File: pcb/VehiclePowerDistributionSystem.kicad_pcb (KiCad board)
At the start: 4 copper layers, 70 x 70 mm, 84 parts, among them J1 B4B-XH-A, J2 B4B-XH-A, J3 B4B-XH-A, J4 B8B-XH-A, J5 B2B-XH-A, J6 FFC2B28-24-G, J7 B2B-XH-A, J8 B2B-XH-A, U1 TMC2209-LA-T, U2 TMC2209-LA-T, U3 TMC2209-LA-T, U4 D24V7F5, U5 D24V7F3, U6 TPS22810DRV, U7 TPS22810DRV

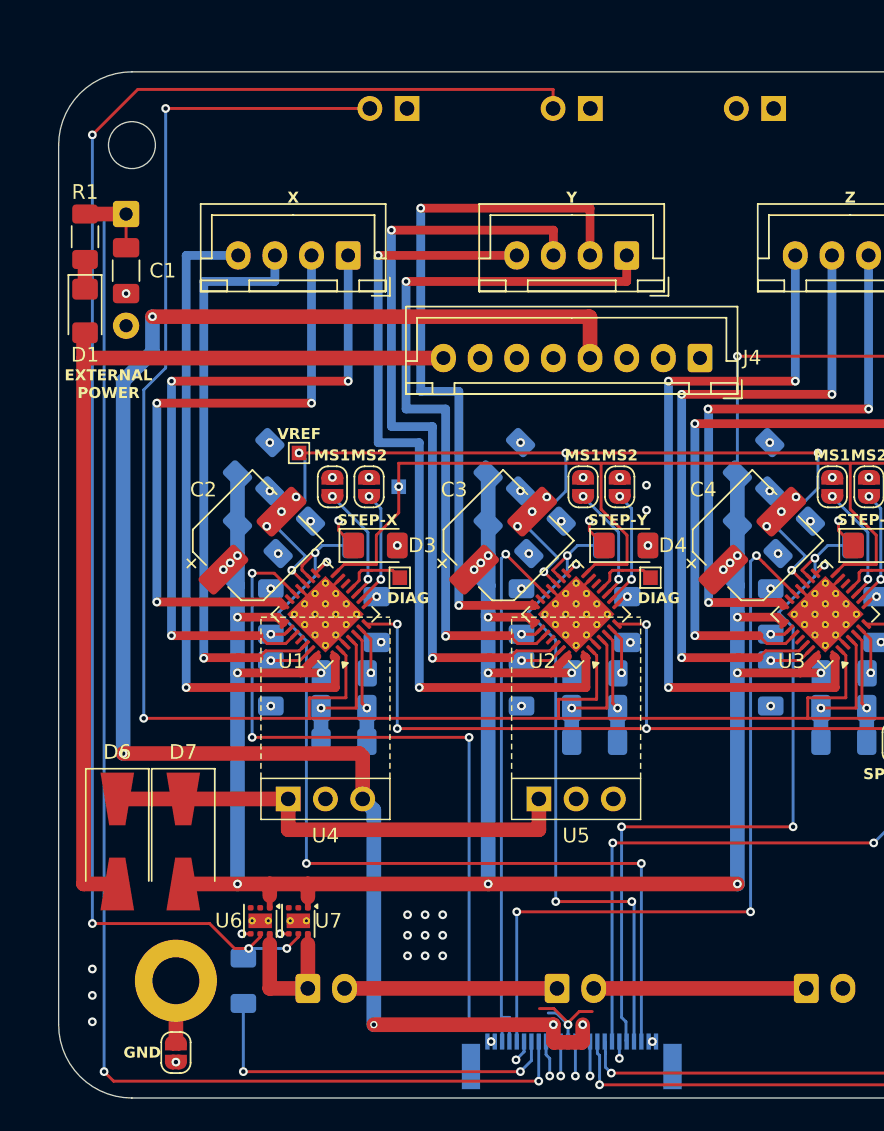
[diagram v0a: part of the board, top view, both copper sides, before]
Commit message: Moved D24V7Fx regulators on `VehiclePowerDistributionSystem` to account for heat-sinks of TMC2209s.
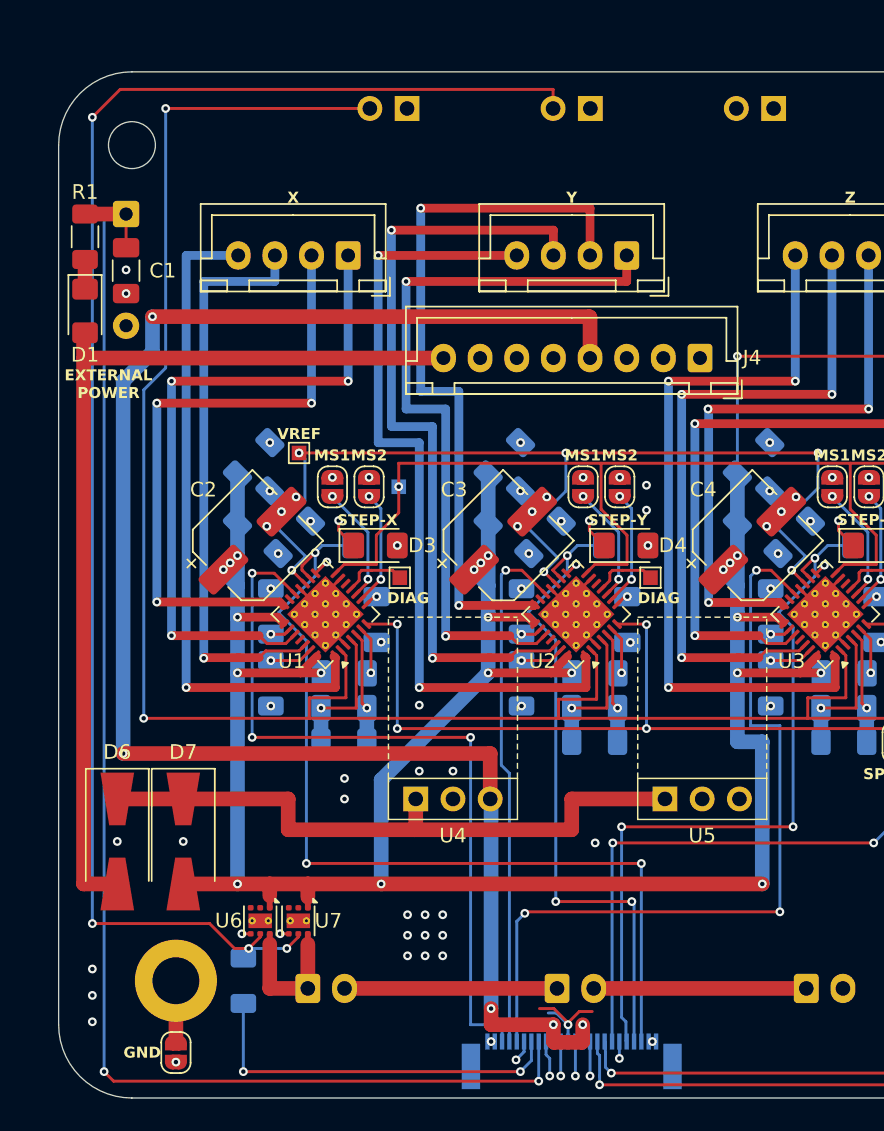
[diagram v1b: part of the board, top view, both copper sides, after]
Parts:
- moved U4 8.70 mm to (141.9, 114.6)
- moved U5 8.60 mm to (158.9, 114.6)
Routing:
- net Net-(D6-K): track 33.0 -> 43.7 mm
- net +MOTOR: track 191.0 -> 197.4 mm
- net motor_direction_z: track 53.0 -> 55.2 mm
- net motor_direction_y: track 37.8 -> 35.9 mm
- net Net-(JP10-B): track 104.4 -> 105.1 mm
- net +5V: track 117.2 -> 117.7 mm
- net +3.3V: vias 30 -> 39

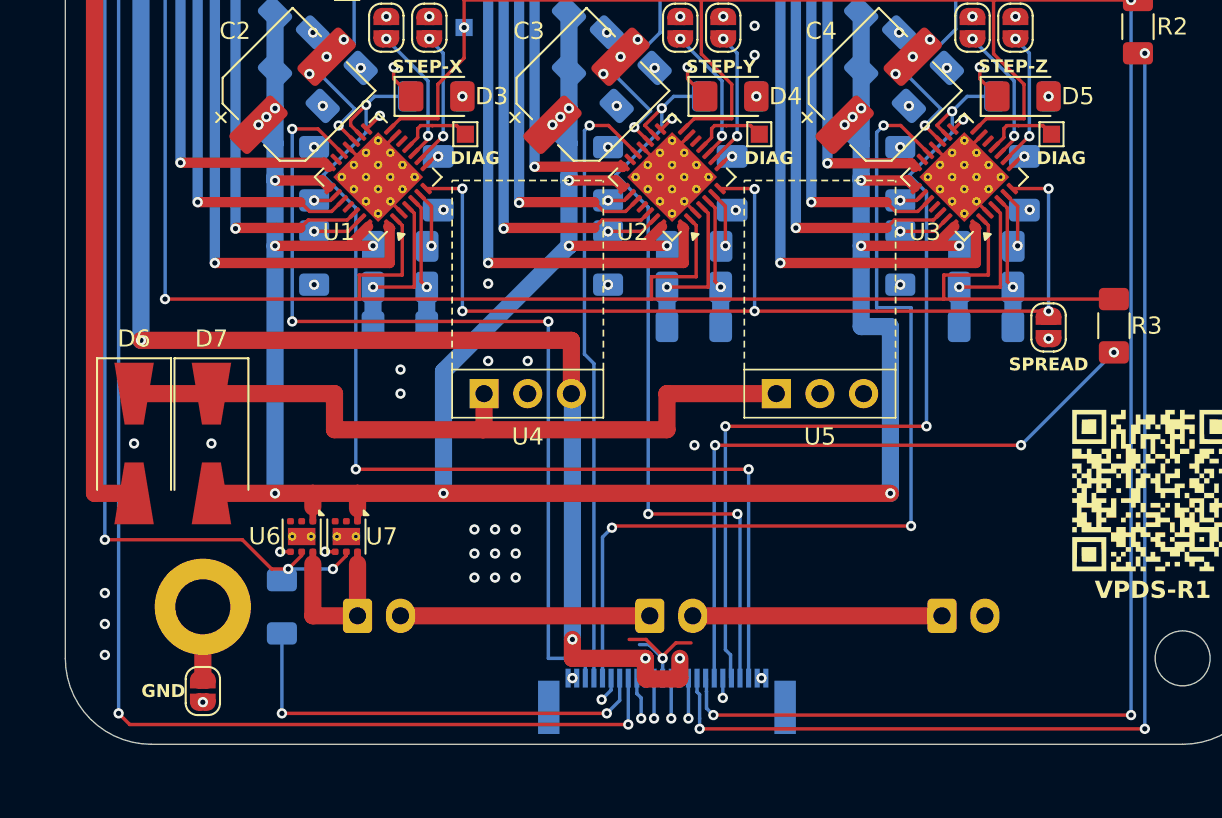
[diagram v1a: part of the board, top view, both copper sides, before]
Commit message: Using `BTS462TATMA1` load-switch instead of `TPS22810DRV`.
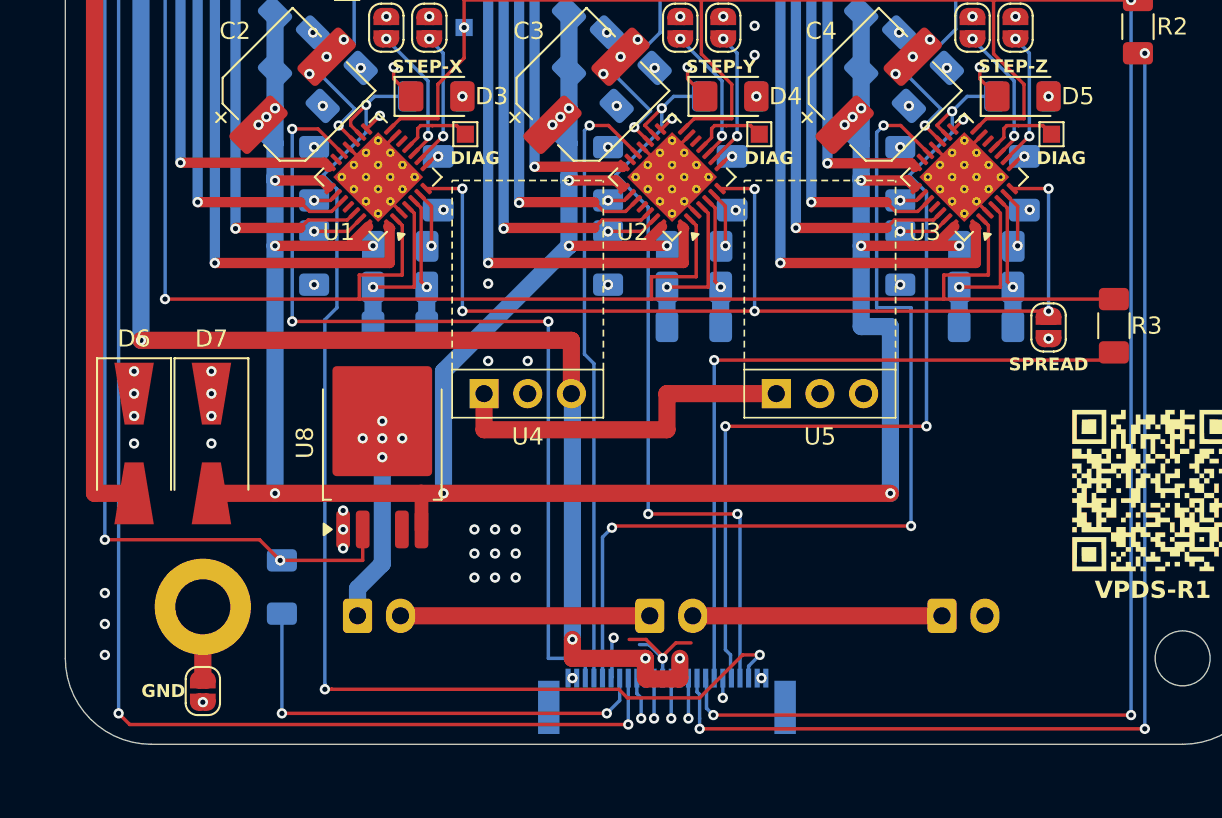
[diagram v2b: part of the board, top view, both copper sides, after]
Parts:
- removed U6, U7: TPS22810DRV, Package_SON:WSON-6-1EP_2x2mm_P0.65mm_EP1x1.6mm_ThermalVias
- added U8: BTS462TATMA1, Package_TO_SOT_SMD:TO-252-4, F.Cu at (133.4, 117.5)
- moved R14 1.15 mm to (127.6, 125.8)
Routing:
- net Net-(D6-K): track 43.7 -> 82.9 mm, vias 0 -> 6
- net Net-(J8-Pin_1): track 10.0 -> 20.6 mm, vias 0 -> 5
- net motor_step_x: track 63.1 -> 68.9 mm
- net motor_disable: track 39.0 -> 41.9 mm, vias 3 -> 1
- net GND: track 43.5 -> 42.3 mm, vias 41 -> 42
- net battery_allowed: track 25.9 -> 27.1 mm
- net +MOTOR: track 197.4 -> 196.3 mm
- net +3.3V: track 12.9 -> 13.8 mm, vias 39 -> 36
- net Net-(JP10-B): track 105.1 -> 105.8 mm, vias 4 -> 3

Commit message: Added pull-up resistor for UART line of TMC2209 drivers.
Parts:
- added R15: 47k, Resistor_SMD:R_1206_3216Metric_Pad1.30x1.75mm_HandSolder, F.Cu at (173.8, 131.4)
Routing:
- net +3.3V: vias 36 -> 37
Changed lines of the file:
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@@
 		)
 	)
+	(footprint "Resistor_SMD:R_1206_3216Metric_Pad1.30x1.75mm_HandSolder"
+		(layer "F.Cu")
+		(at 173.8 131.449999 -90)
+		(descr "Resistor SMD 1206 (3216 Metric), square (rectangular) end terminal, IPC-7351 nominal with elongated pad for handsoldering. (Body size source: IPC-SM-782 page 72, https://www.pcb-3d.com/wordpress/wp-content/uploads/ipc-sm-782a_amendment_1_and_2.pdf), generated with kicad-footprint-generator")
+		(tags "resistor handsolder")
+		(property "Reference" "R15"
+			(at 0 -1.829999 90)
+			(layer "F.SilkS")
+			(effects
+				(font
+					(size 1 1)
+					(thickness 0.15)
+				)
+			)
+		)
+		(property "Value" "47k"
+			(at 0 1.829999 90)
+			(layer "F.Fab")
+			(effects
+				(font
+					(size 1 1)
+					(thickness 0.15)
+				)
+			)
+		)
+		(property "Datasheet" "~"
+			(at 0 0 90)
+			(layer "F.Fab")
+			(hide yes)
+			(effects
+				(font
+					(size 1.27 1.27)
+					(thickness 0.15)
+				)
+			)
+		)
+		(property "Description" "Resistor"
+			(at 0 0 90)
+			(layer "F.Fab")
+			(hide yes)
+			(effects
+				(font
+					(size 1.27 1.27)
+					(thickness 0.15)
+				)
+			)
+		)
+		(property ki_fp_filters "R_*")
+		(sheetname "/")
+		(sheetfile "VehiclePowerDistributionSystem.kicad_sch")
+		(attr smd)
+		(fp_line
+			(start -0.727064 0.91)
+			(end 0.727064 0.91)
+			(stroke
+				(width 0.12)
+				(type solid)
+			)
+			(layer "F.SilkS")
+		)
+		(fp_line
+			(start -0.727064 -0.91)
+			(end 0.727064 -0.91)
+			(stroke
+				(width 0.12)
+				(type solid)
+			)
+			(layer "F.SilkS")
+		)
+		(fp_line
+			(start -2.45 1.13)
+			(end -2.45 -1.13)
+			(stroke
+				(width 0.05)
+				(type solid)
+			)
+			(layer "F.CrtYd")
+		)
+		(fp_line
+			(start 2.45 1.13)
+			(end -2.45 1.13)
+			(stroke
+				(width 0.05)
+				(type solid)
+			)
+			(layer "F.CrtYd")
+		)
+		(fp_line
+			(start -2.45 -1.13)
+			(end 2.45 -1.13)
+			(stroke
+				(width 0.05)
+				(type solid)
+			)
+			(layer "F.CrtYd")
+		)
+		(fp_line
+			(start 2.45 -1.13)
+			(end 2.45 1.13)
+			(stroke
+				(width 0.05)
+				(type solid)
+			)
+			(layer "F.CrtYd")
+		)
+		(fp_line
+			(start -1.6 0.8)
+			(end -1.6 -0.8)
+			(stroke
+				(width 0.1)
+				(type solid)
+			)
+			(layer "F.Fab")
+		)
+		(fp_line
+			(start 1.6 0.8)
+			(end -1.6 0.8)
+			(stroke
+				(width 0.1)
+				(type solid)
+			)
+			(layer "F.Fab")
+		)
+		(fp_line
+			(start -1.6 -0.8)
+			(end 1.6 -0.8)
+			(stroke
+				(width 0.1)
+				(type solid)
+			)
+			(layer "F.Fab")
+		)
+		(fp_line
+			(start 1.6 -0.8)
+			(end 1.6 0.8)
+			(stroke
+				(width 0.1)
+				(type solid)
+			)
+			(layer "F.Fab")
+		)
+		(fp_text user "${REFERENCE}"
+			(at 0 0 90)
+			(layer "F.Fab")
+			(effects
+				(font
+					(size 0.8 0.8)
+					(thickness 0.12)
+				)
+			)
+		)
+		(pad "1" smd roundrect
+			(at -1.550001 0 270)
+			(size 1.3 1.75)
+			(layers "F.Cu" "F.Mask" "F.Paste")
+			(roundrect_rratio 0.192308)
+			(net 2 "+3.3V")
+			(pintype "passive")
+		)
+		(pad "2" smd roundrect
+			(at 1.550001 0 270)
+			(size 1.3 1.75)
+			(layers "F.Cu" "F.Mask" "F.Paste")
+			(roundrect_rratio 0.192308)
+			(net 47 "motor_uart_rx")
+			(pintype "passive")
+		)
+		(embedded_fonts no)
+		(model "${KICAD9_3DMODEL_DIR}/Resistor_SMD.3dshapes/R_1206_3216Metric.step"
+			(offset
+				(xyz 0 0 0)
+			)
+			(scale
+				(xyz 1 1 1)
+			)
+			(rotate
+				(xyz 0 0 0)
+			)
+		)
+	)
 	(footprint "pcb:Dummy"
 		(locked yes)
@@
 		(net 2)
 	)
+	(via
+		(at 173.8 129.899998)
+		(size 0.6)
+		(drill 0.3)
+		(layers "F.Cu" "B.Cu")
+		(net 2)
+	)

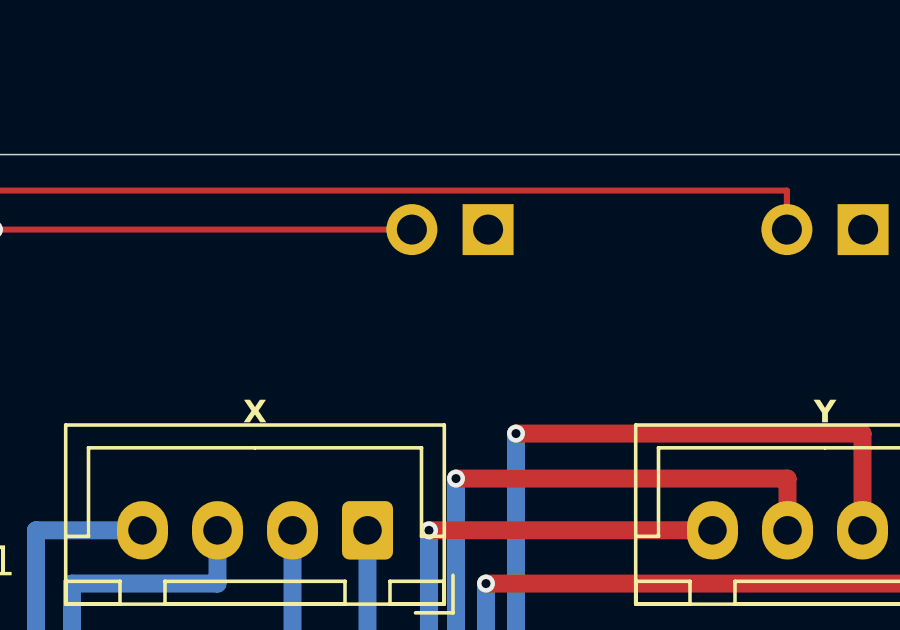
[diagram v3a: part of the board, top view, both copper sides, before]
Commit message: Added pull-up for TMC2209 enable pins.
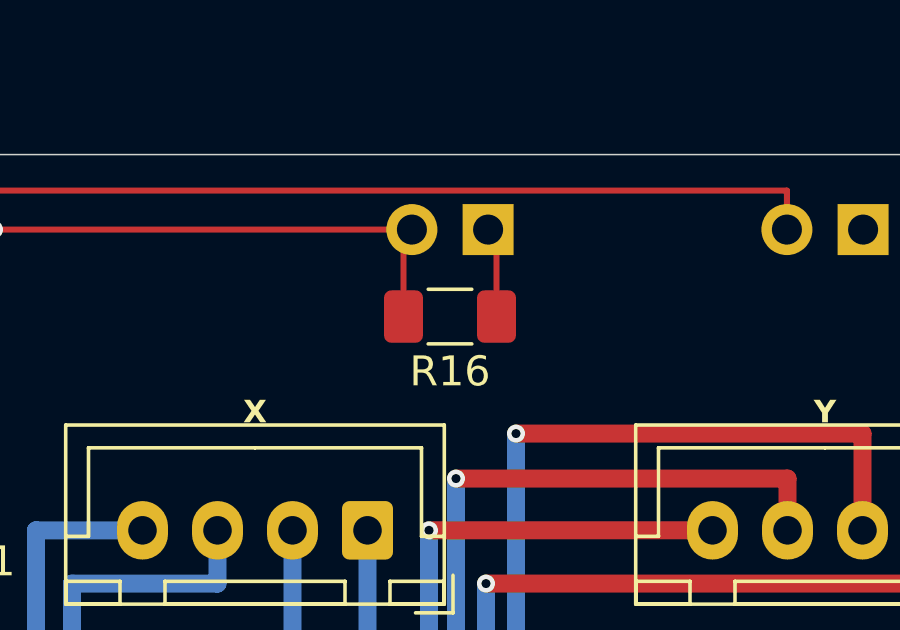
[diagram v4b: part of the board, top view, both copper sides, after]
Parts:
- added R16: 47k, Resistor_SMD:R_1206_3216Metric_Pad1.30x1.75mm_HandSolder, F.Cu at (137.5, 70.4)
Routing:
- net /Stepper Motor Driver - X/DISABLE: track 133.5 -> 136.6 mm
- net +3.3V: track 13.8 -> 16.9 mm
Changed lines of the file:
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@@
 		)
 	)
+	(footprint "Resistor_SMD:R_1206_3216Metric_Pad1.30x1.75mm_HandSolder"
+		(layer "F.Cu")
+		(at 137.5 70.4 180)
+		(descr "Resistor SMD 1206 (3216 Metric), square (rectangular) end terminal, IPC-7351 nominal with elongated pad for handsoldering. (Body size source: IPC-SM-782 page 72, https://www.pcb-3d.com/wordpress/wp-content/uploads/ipc-sm-782a_amendment_1_and_2.pdf), generated with kicad-footprint-generator")
+		(tags "resistor handsolder")
+		(property "Reference" "R16"
+			(at 0 -1.829999 0)
+			(layer "F.SilkS")
+			(effects
+				(font
+					(size 1 1)
+					(thickness 0.15)
+				)
+			)
+		)
+		(property "Value" "47k"
+			(at 0 1.829999 0)
+			(layer "F.Fab")
+			(effects
+				(font
+					(size 1 1)
+					(thickness 0.15)
+				)
+			)
+		)
+		(property "Datasheet" "~"
+			(at 0 0 0)
+			(layer "F.Fab")
+			(hide yes)
+			(effects
+				(font
+					(size 1.27 1.27)
+					(thickness 0.15)
+				)
+			)
+		)
+		(property "Description" "Resistor"
+			(at 0 0 0)
+			(layer "F.Fab")
+			(hide yes)
+			(effects
+				(font
+					(size 1.27 1.27)
+					(thickness 0.15)
+				)
+			)
+		)
+		(property ki_fp_filters "R_*")
+		(sheetname "/")
+		(sheetfile "VehiclePowerDistributionSystem.kicad_sch")
+		(attr smd)
+		(fp_line
+			(start -0.727064 0.91)
+			(end 0.727064 0.91)
+			(stroke
+				(width 0.12)
+				(type solid)
+			)
+			(layer "F.SilkS")
+		)
+		(fp_line
+			(start -0.727064 -0.91)
+			(end 0.727064 -0.91)
+			(stroke
+				(width 0.12)
+				(type solid)
+			)
+			(layer "F.SilkS")
+		)
+		(fp_line
+			(start 2.45 1.13)
+			(end -2.45 1.13)
+			(stroke
+				(width 0.05)
+				(type solid)
+			)
+			(layer "F.CrtYd")
+		)
+		(fp_line
+			(start 2.45 -1.13)
+			(end 2.45 1.13)
+			(stroke
+				(width 0.05)
+				(type solid)
+			)
+			(layer "F.CrtYd")
+		)
+		(fp_line
+			(start -2.45 1.13)
+			(end -2.45 -1.13)
+			(stroke
+				(width 0.05)
+				(type solid)
+			)
+			(layer "F.CrtYd")
+		)
+		(fp_line
+			(start -2.45 -1.13)
+			(end 2.45 -1.13)
+			(stroke
+				(width 0.05)
+				(type solid)
+			)
+			(layer "F.CrtYd")
+		)
+		(fp_line
+			(start 1.6 0.8)
+			(end -1.6 0.8)
+			(stroke
+				(width 0.1)
+				(type solid)
+			)
+			(layer "F.Fab")
+		)
+		(fp_line
+			(start 1.6 -0.8)
+			(end 1.6 0.8)
+			(stroke
+				(width 0.1)
+				(type solid)
+			)
+			(layer "F.Fab")
+		)
+		(fp_line
+			(start -1.6 0.8)
+			(end -1.6 -0.8)
+			(stroke
+				(width 0.1)
+				(type solid)
+			)
+			(layer "F.Fab")
+		)
+		(fp_line
+			(start -1.6 -0.8)
+			(end 1.6 -0.8)
+			(stroke
+				(width 0.1)
+				(type solid)
+			)
+			(layer "F.Fab")
+		)
+		(fp_text user "${REFERENCE}"
+			(at 0 0 0)
+			(layer "F.Fab")
+			(effects
+				(font
+					(size 0.8 0.8)
+					(thickness 0.12)
+				)
+			)
+		)
+		(pad "1" smd roundrect
+			(at -1.550001 0 180)
+			(size 1.3 1.75)
+			(layers "F.Cu" "F.Mask" "F.Paste")
+			(roundrect_rratio 0.192308)
+			(net 2 "+3.3V")
+			(pintype "passive")
+		)
+		(pad "2" smd roundrect
+			(at 1.550001 0 180)
+			(size 1.3 1.75)
+			(layers "F.Cu" "F.Mask" "F.Paste")
+			(roundrect_rratio 0.192308)
+			(net 5 "/Stepper Motor Driver - X/DISABLE")
+			(pintype "passive")
+		)
+		(embedded_fonts no)
+		(model "${KICAD9_3DMODEL_DIR}/Resistor_SMD.3dshapes/R_1206_3216Metric.step"
+			(offset
+				(xyz 0 0 0)
+			)
+			(scale
+				(xyz 1 1 1)
+			)
+			(rotate
+				(xyz 0 0 0)
+			)
+		)
+	)
 	(footprint "Connector_JST:JST_XH_B4B-XH-A_1x04_P2.50mm_Vertical"
 		(locked yes)
@@
 	)
 	(segment
+		(start 139.050001 67.780001)
+		(end 138.77 67.5)
+		(width 0.2)
+		(layer "F.Cu")
+		(net 2)
+	)
+	(segment
 		(start 148.781785 128.9)
 		(end 147.8 128.9)
@@
 	)
 	(segment
+		(start 139.050001 70.4)
+		(end 139.050001 67.780001)
+		(width 0.2)
+		(layer "F.Cu")
+		(net 2)
+	)
+	(segment
 		(start 133.3 98.435176)
 		(end 132.52825 99.206926)
@@
 		(end 136.23 67.5)
 		(width 0.2)
+		(layer "F.Cu")
+		(net 5)
+	)
+	(segment
+		(start 135.949999 70.4)
+		(end 135.949999 67.780001)
+		(width 0.2)
+		(layer "F.Cu")
+		(net 5)
+	)
+	(segment
+		(start 135.949999 67.780001)
+		(end 136.23 67.5)
+		(width 0.2)
